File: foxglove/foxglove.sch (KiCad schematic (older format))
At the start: 50 parts, among them J1 NEIGHBOR1, J2 NEIGHBOR2, J3 Conn_02x05_Odd_Even, J4 Conn_02x05_Odd_Even, J5 Conn_01x02_Female, J7 BONUS_ROW, U1 ICE40HX8K-CT256, U2 TLV711, U3 MC4558CPT, U4 74LVC1G3157, U5 LM339, U6 ADP225, U7 DAC084S085, U8 74AHC1G04

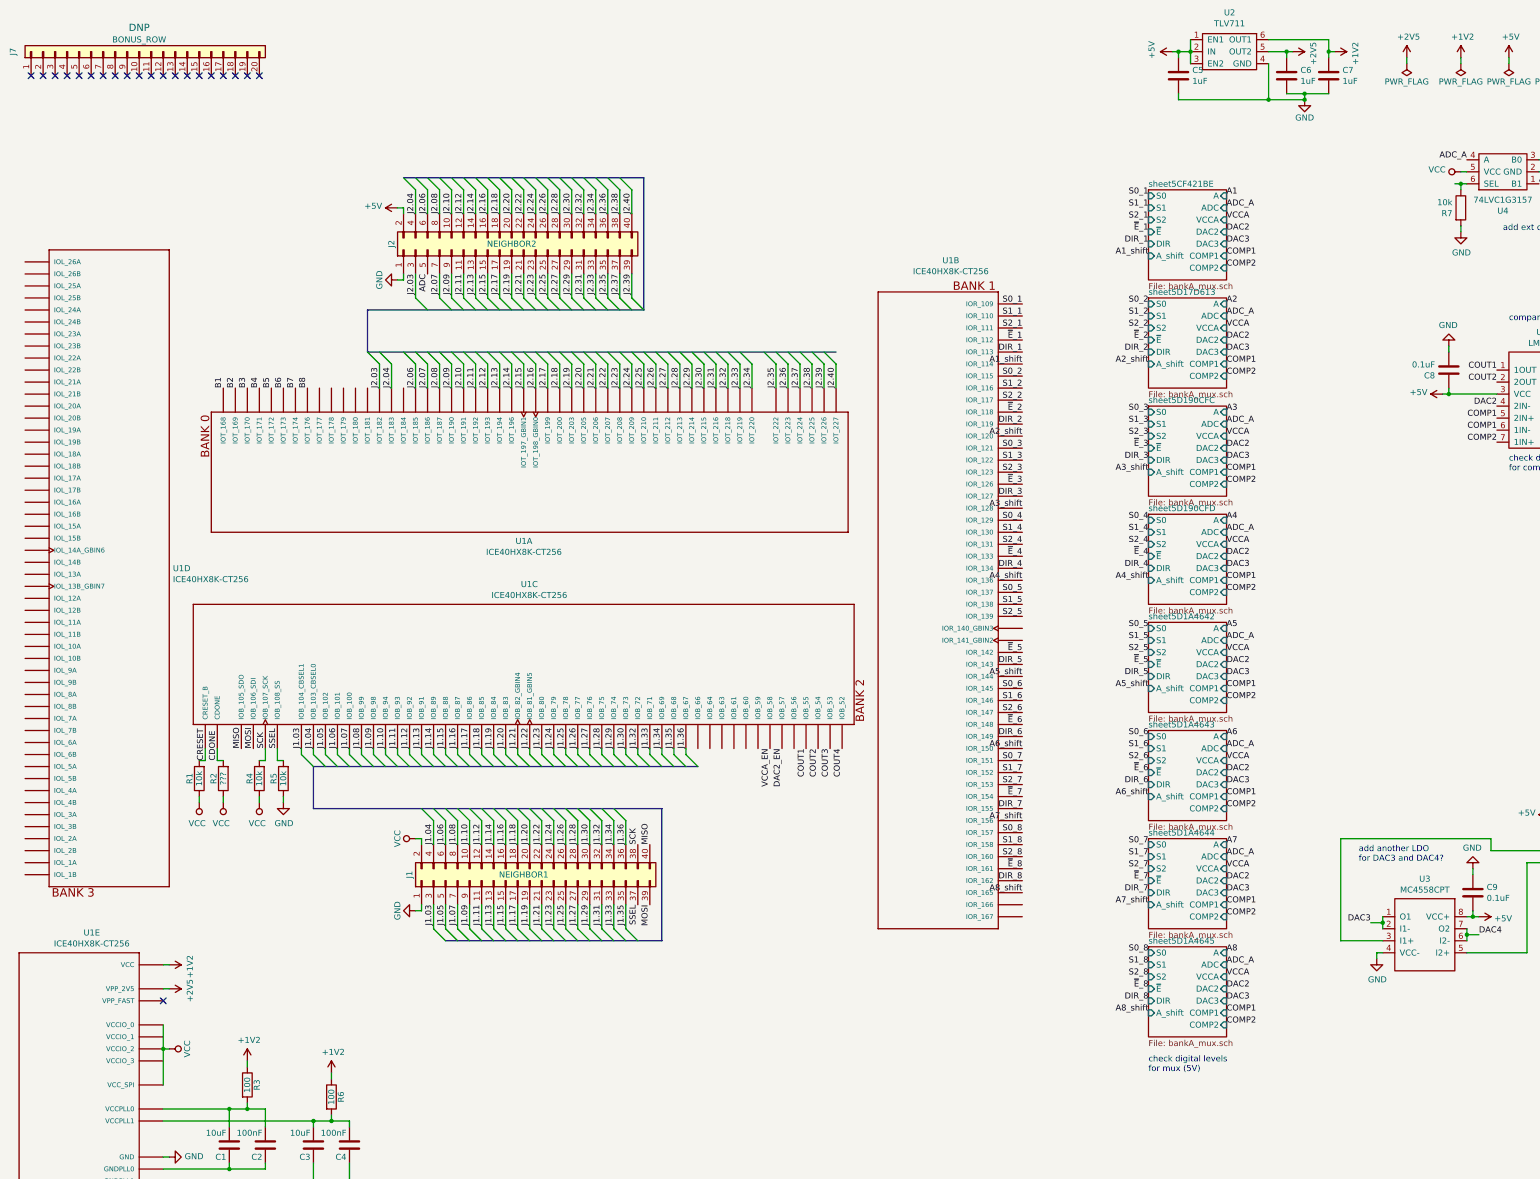
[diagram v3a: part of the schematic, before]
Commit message: Routed FPGA connections to J2 connector
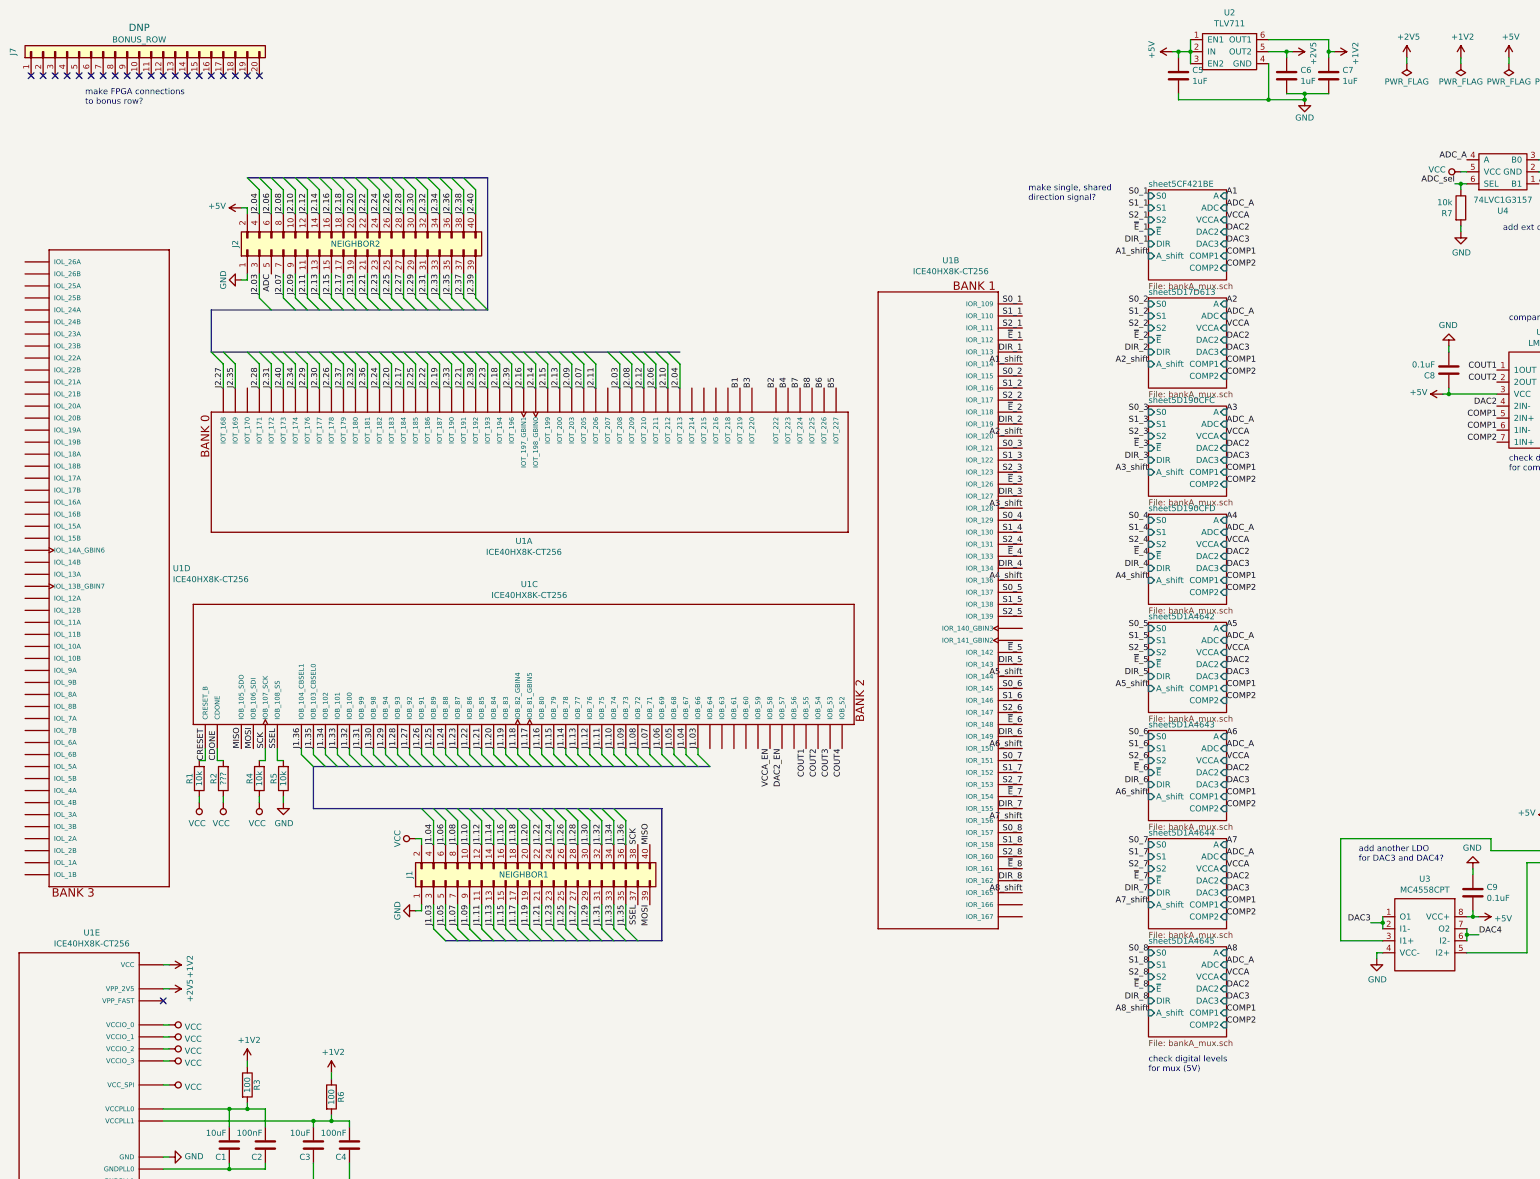
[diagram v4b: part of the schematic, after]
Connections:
- net B1: now also U1.D5 (IOT_219); no longer U1.C14 (IOT_168)
- net B2: now also U1.C4 (IOT_222); no longer U1.B15 (IOT_169)
- net B3: now also U1.A1 (IOT_220); no longer U1.D13 (IOT_170)
- net B4: now also U1.B3 (IOT_223); no longer U1.B14 (IOT_171)
- net B5: now also U1.C3 (IOT_227); no longer U1.C12 (IOT_172)
- net B6: now also U1.D3 (IOT_226); no longer U1.E11 (IOT_173)
- net B7: now also U1.D4 (IOT_224); no longer U1.C13 (IOT_174)
- net B8: now also U1.E5 (IOT_225); no longer U1.A16 (IOT_176)
- net J1.03: now also U1.N7 (IOB_66); no longer U1.P13 (IOB_104_CBSEL1)
- net J1.04: now also U1.P6 (IOB_67); no longer U1.K11 (IOB_103_CBSEL0)
- net J1.05: now also U1.M8 (IOB_68); no longer U1.R16 (IOB_102)
- net J1.06: now also U1.T5 (IOB_69); no longer U1.M12 (IOB_101)
- net J1.07: now also U1.R6 (IOB_71); no longer U1.T16 (IOB_100)
- net J1.08: now also U1.P8 (IOB_72); no longer U1.L11 (IOB_99)
- net J1.09: now also U1.T6 (IOB_73); no longer U1.N12 (IOB_98)
- net J1.10: now also U1.L9 (IOB_74); no longer U1.T13 (IOB_94)
- net J1.11: now also U1.T7 (IOB_75); no longer U1.M11 (IOB_93)
- net J1.12: now also U1.T8 (IOB_76); no longer U1.T14 (IOB_92)
- net J1.13: now also U1.P7 (IOB_77); no longer U1.T15 (IOB_91)
- net J1.14: now also U1.N9 (IOB_78); no longer U1.T11 (IOB_89)
- net J1.15: now also U1.T9 (IOB_79); no longer U1.T10 (IOB_88)
- net J1.16: now also U1.M9 (IOB_80); no longer U1.N10 (IOB_87)
- net J1.17: now also U1.R9 (IOB_81_GBIN5); no longer U1.P10 (IOB_86)
- net J1.18: now also U1.K9 (IOB_82_GBIN4); no longer U1.L10 (IOB_85)
- net J1.19: now also U1.P9 (IOB_83); no longer U1.R10 (IOB_84)
- net J1.20: now also U1.R10 (IOB_84); no longer U1.P9 (IOB_83)
- net J1.21: now also U1.L10 (IOB_85); no longer U1.K9 (IOB_82_GBIN4)
- net J1.22: now also U1.P10 (IOB_86); no longer U1.R9 (IOB_81_GBIN5)
- net J1.23: now also U1.N10 (IOB_87); no longer U1.M9 (IOB_80)
- net J1.24: now also U1.T10 (IOB_88); no longer U1.T9 (IOB_79)
- net J1.25: now also U1.T11 (IOB_89); no longer U1.N9 (IOB_78)
- net J1.26: now also U1.T15 (IOB_91); no longer U1.P7 (IOB_77)
- net J1.27: now also U1.T14 (IOB_92); no longer U1.T8 (IOB_76)
- net J1.28: now also U1.M11 (IOB_93); no longer U1.T7 (IOB_75)
- net J1.29: now also U1.T13 (IOB_94); no longer U1.L9 (IOB_74)
- net J1.30: now also U1.N12 (IOB_98); no longer U1.T6 (IOB_73)
- net J1.31: now also U1.L11 (IOB_99)
- net J1.32: now also U1.T16 (IOB_100); no longer U1.P8 (IOB_72)
- net J1.33: now also U1.M12 (IOB_101); no longer U1.R6 (IOB_71)
- net J1.34: now also U1.R16 (IOB_102); no longer U1.T5 (IOB_69)
- net J1.35: now also U1.K11 (IOB_103_CBSEL0); no longer U1.M8 (IOB_68)
- net J1.36: now also U1.P13 (IOB_104_CBSEL1); no longer U1.P6 (IOB_67)
- net J2.03: now also U1.B6 (IOT_208); no longer U1.B12 (IOT_182)
- net J2.04: now also U1.A5 (IOT_213); no longer U1.B10 (IOT_183)
- net J2.06: now also U1.A6 (IOT_211); no longer U1.C10 (IOT_185)
- net J2.07: now also U1.A7 (IOT_205); no longer U1.A10 (IOT_186)
- net J2.08: now also U1.C6 (IOT_209); no longer U1.A11 (IOT_187)
- net J2.09: now also U1.B8 (IOT_203); no longer U1.D10 (IOT_190)
- net J2.10: now also U1.D6 (IOT_212); no longer U1.C9 (IOT_191)
- net J2.11: now also U1.C7 (IOT_206); no longer U1.E9 (IOT_192)
- net J2.12: now also U1.D7 (IOT_210); no longer U1.D9 (IOT_193)
- net J2.13: now also U1.D8 (IOT_200); no longer U1.A9 (IOT_194)
- net J2.14: now also U1.F7 (IOT_198_GBIN0); no longer U1.F9 (IOT_196)
- net J2.15: now also U1.B9 (IOT_199); no longer U1.C8 (IOT_197_GBIN1)
- net J2.16: now also U1.C8 (IOT_197_GBIN1); no longer U1.F7 (IOT_198_GBIN0)
- net J2.17: now also U1.B11 (IOT_184); no longer U1.B9 (IOT_199)
- net J2.18: now also U1.A9 (IOT_194); no longer U1.D8 (IOT_200)
- net J2.19: now also U1.A11 (IOT_187); no longer U1.B8 (IOT_203)
- net J2.20: now also U1.B10 (IOT_183); no longer U1.A7 (IOT_205)
- net J2.21: now also U1.C9 (IOT_191); no longer U1.C7 (IOT_206)
- net J2.22: now also U1.A10 (IOT_186); no longer U1.B7 (IOT_207)
- net J2.23: now also U1.D9 (IOT_193); no longer U1.B6 (IOT_208)
- net J2.24: now also U1.B12 (IOT_182); no longer U1.C6 (IOT_209)
- net J2.25: now also U1.C10 (IOT_185); no longer U1.D7 (IOT_210)
- net J2.26: now also U1.B13 (IOT_178); no longer U1.A6 (IOT_211)
- net J2.27: now also U1.C14 (IOT_168); no longer U1.D6 (IOT_212)
- net J2.28: now also U1.B14 (IOT_171); no longer U1.A5 (IOT_213)
- net J2.29: now also U1.A16 (IOT_176); no longer U1.B5 (IOT_214)
- net J2.30: now also U1.A15 (IOT_177); no longer U1.E6 (IOT_215)
- net J2.31: now also U1.C12 (IOT_172); no longer U1.B4 (IOT_216)
- net J2.32: now also U1.C11 (IOT_180); no longer U1.A2 (IOT_218)
- net J2.33: now also U1.D10 (IOT_190); no longer U1.D5 (IOT_219)
- net J2.34: now also U1.C13 (IOT_174); no longer U1.A1 (IOT_220)
- net J2.35: now also U1.B15 (IOT_169); no longer U1.C4 (IOT_222)
- net J2.36: now also U1.D11 (IOT_181); no longer U1.B3 (IOT_223)
- net J2.37: now also U1.E10 (IOT_179); no longer U1.D4 (IOT_224)
- net J2.38: now also U1.E9 (IOT_192); no longer U1.E5 (IOT_225)
- net J2.39: now also U1.F9 (IOT_196); no longer U1.D3 (IOT_226)
- net J2.40: now also U1.E11 (IOT_173); no longer U1.C3 (IOT_227)
- net VCC: now also U1.C15 (VCCIO_1), U1.E1 (VCCIO_3), U1.G6 (VCCIO_3), U1.H10 (VCCIO_1), U1.H15 (VCCIO_1), U1.J6 (VCCIO_3), U1.N1 (VCCIO_3), U1.N15 (VCCIO_1)
- net ADC_sel: now reaches R7.1, U4.6 (SEL)
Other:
- note added: "make FPGA connections \nto bonus row?"
- note added: "make single, shared\ndirection signal?"
- moved on the sheet: J2

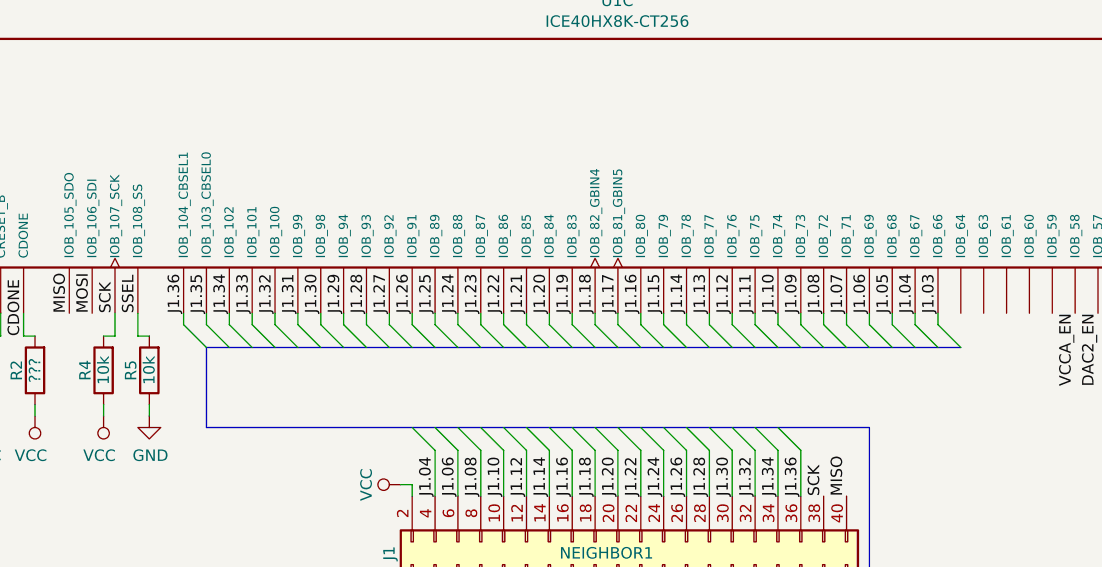
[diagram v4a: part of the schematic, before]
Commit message: Foxglove: Routed FPGA to J1 header
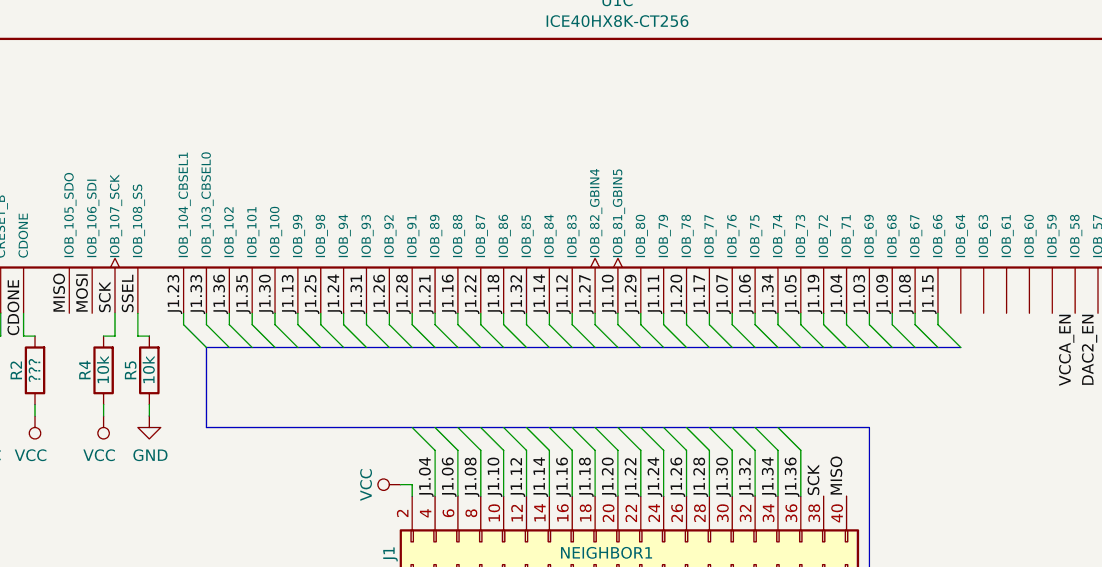
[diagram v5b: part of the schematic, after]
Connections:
- net J1.03: now also U1.T5 (IOB_69); no longer U1.N7 (IOB_66)
- net J1.04: now also U1.R6 (IOB_71); no longer U1.P6 (IOB_67)
- net J1.05: now also U1.T6 (IOB_73); no longer U1.M8 (IOB_68)
- net J1.06: now also U1.T7 (IOB_75); no longer U1.T5 (IOB_69)
- net J1.07: now also U1.T8 (IOB_76); no longer U1.R6 (IOB_71)
- net J1.08: now also U1.P6 (IOB_67); no longer U1.P8 (IOB_72)
- net J1.09: now also U1.M8 (IOB_68); no longer U1.T6 (IOB_73)
- net J1.10: now also U1.R9 (IOB_81_GBIN5); no longer U1.L9 (IOB_74)
- net J1.11: now also U1.T9 (IOB_79); no longer U1.T7 (IOB_75)
- net J1.12: now also U1.P9 (IOB_83); no longer U1.T8 (IOB_76)
- net J1.13: now also U1.L11 (IOB_99); no longer U1.P7 (IOB_77)
- net J1.14: now also U1.R10 (IOB_84); no longer U1.N9 (IOB_78)
- net J1.15: now also U1.N7 (IOB_66); no longer U1.T9 (IOB_79)
- net J1.16: now also U1.T10 (IOB_88); no longer U1.M9 (IOB_80)
- net J1.17: now also U1.P7 (IOB_77); no longer U1.R9 (IOB_81_GBIN5)
- net J1.18: now also U1.P10 (IOB_86); no longer U1.K9 (IOB_82_GBIN4)
- net J1.19: now also U1.P8 (IOB_72); no longer U1.P9 (IOB_83)
- net J1.20: now also U1.N9 (IOB_78); no longer U1.R10 (IOB_84)
- net J1.21: now also U1.T11 (IOB_89); no longer U1.L10 (IOB_85)
- net J1.22: now also U1.N10 (IOB_87); no longer U1.P10 (IOB_86)
- net J1.23: now also U1.P13 (IOB_104_CBSEL1); no longer U1.N10 (IOB_87)
- net J1.24: now also U1.T13 (IOB_94); no longer U1.T10 (IOB_88)
- net J1.25: now also U1.N12 (IOB_98); no longer U1.T11 (IOB_89)
- net J1.26: now also U1.T14 (IOB_92); no longer U1.T15 (IOB_91)
- net J1.27: now also U1.K9 (IOB_82_GBIN4); no longer U1.T14 (IOB_92)
- net J1.28: now also U1.T15 (IOB_91); no longer U1.M11 (IOB_93)
- net J1.29: now also U1.M9 (IOB_80); no longer U1.T13 (IOB_94)
- net J1.30: now also U1.T16 (IOB_100); no longer U1.N12 (IOB_98)
- net J1.31: now also U1.M11 (IOB_93); no longer U1.L11 (IOB_99)
- net J1.32: now also U1.L10 (IOB_85); no longer U1.T16 (IOB_100)
- net J1.33: now also U1.K11 (IOB_103_CBSEL0); no longer U1.M12 (IOB_101)
- net J1.34: now also U1.L9 (IOB_74); no longer U1.R16 (IOB_102)
- net J1.35: now also U1.M12 (IOB_101); no longer U1.K11 (IOB_103_CBSEL0)
- net J1.36: now also U1.R16 (IOB_102); no longer U1.P13 (IOB_104_CBSEL1)
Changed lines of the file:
@@
 Text Label 5750 7450 1    50   ~ 0
 J1.36
+Text Label 3250 6650 1    50   ~ 0
+J1.36
+Text Label 3350 6650 1    50   ~ 0
+J1.35
+Text Label 5650 6650 1    50   ~ 0
+J1.34
+Text Label 3150 6650 1    50   ~ 0
+J1.33
+Text Label 4550 6650 1    50   ~ 0
+J1.32
+Text Label 3850 6650 1    50   ~ 0
+J1.31
+Text Label 3450 6650 1    50   ~ 0
+J1.30
+Text Label 5050 6650 1    50   ~ 0
+J1.29
+Text Label 4050 6650 1    50   ~ 0
+J1.28
+Text Label 4850 6650 1    50   ~ 0
+J1.27
+Text Label 3950 6650 1    50   ~ 0
+J1.26
+Text Label 3650 6650 1    50   ~ 0
+J1.25
+Text Label 3750 6650 1    50   ~ 0
+J1.24
 Text Label 3050 6650 1    50   ~ 0
-J1.36
-Text Label 3150 6650 1    50   ~ 0
-J1.35
-Text Label 3250 6650 1    50   ~ 0
-J1.34
-Text Label 3350 6650 1    50   ~ 0
-J1.33
-Text Label 3450 6650 1    50   ~ 0
-J1.32
+J1.23
+Text Label 4350 6650 1    50   ~ 0
+J1.22
+Text Label 4150 6650 1    50   ~ 0
+J1.21
+Text Label 5250 6650 1    50   ~ 0
+J1.20
+Text Label 5850 6650 1    50   ~ 0
+J1.19
+Text Label 4450 6650 1    50   ~ 0
+J1.18
+Text Label 5350 6650 1    50   ~ 0
+J1.17
+Text Label 4250 6650 1    50   ~ 0
+J1.16
+Text Label 6350 6650 1    50   ~ 0
+J1.15
+Text Label 4650 6650 1    50   ~ 0
+J1.14
 Text Label 3550 6650 1    50   ~ 0
-J1.31
-Text Label 3650 6650 1    50   ~ 0
-J1.30
-Text Label 3750 6650 1    50   ~ 0
-J1.29
-Text Label 3850 6650 1    50   ~ 0
-J1.28
-Text Label 3950 6650 1    50   ~ 0
-J1.27
-Text Label 4050 6650 1    50   ~ 0
-J1.26
-Text Label 4150 6650 1    50   ~ 0
-J1.25
-Text Label 4250 6650 1    50   ~ 0
-J1.24
-Text Label 4350 6650 1    50   ~ 0
-J1.23
-Text Label 4450 6650 1    50   ~ 0
-J1.22
-Text Label 4550 6650 1    50   ~ 0
-J1.21
-Text Label 4650 6650 1    50   ~ 0
-J1.20
+J1.13
 Text Label 4750 6650 1    50   ~ 0
-J1.19
-Text Label 4850 6650 1    50   ~ 0
-J1.18
+J1.12
+Text Label 5150 6650 1    50   ~ 0
+J1.11
 Text Label 4950 6650 1    50   ~ 0
-J1.17
-Text Label 5050 6650 1    50   ~ 0
-J1.16
-Text Label 5150 6650 1    50   ~ 0
-J1.15
-Text Label 5250 6650 1    50   ~ 0
-J1.14
-Text Label 5350 6650 1    50   ~ 0
-J1.13
+J1.10
+Text Label 6150 6650 1    50   ~ 0
+J1.09
+Text Label 6250 6650 1    50   ~ 0
+J1.08
 Text Label 5450 6650 1    50   ~ 0
-J1.12
+J1.07
 Text Label 5550 6650 1    50   ~ 0
-J1.11
-Text Label 5650 6650 1    50   ~ 0
-J1.10
+J1.06
 Text Label 5750 6650 1    50   ~ 0
-J1.09
-Text Label 5850 6650 1    50   ~ 0
-J1.08
+J1.05
 Text Label 5950 6650 1    50   ~ 0
-J1.07
-Text Label 6050 6650 1    50   ~ 0
-J1.06
-Text Label 6150 6650 1    50   ~ 0
-J1.05
-Text Label 6250 6650 1    50   ~ 0
 J1.04
 Entry Wire Line
@@
 	15100 7500 15050 7500
 Connection ~ 15050 7500
-Text Label 6350 6650 1    50   ~ 0
+Text Label 6050 6650 1    50   ~ 0
 J1.03
 Entry Wire Line
@@
 Wire Wire Line
 	1900 9150 1950 9150
+Text Notes 9100 2100 0    50   ~ 0
+make single, shared\ndirection signal?
 Wire Bus Line
 	2600 1900 4600 1900
@@
 Wire Bus Line
 	3150 6800 6450 6800
-Text Notes 9100 2100 0    50   ~ 0
-make single, shared\ndirection signal?
 $EndSCHEMATC
